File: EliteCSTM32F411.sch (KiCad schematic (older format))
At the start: 27 parts, among them SW1 Boot Mode, SW2 Reset Switch, U1 STM32F411CEUx, U2 XC6206PxxxMR, U3 Elite-C, Y1 8Mhz 3225

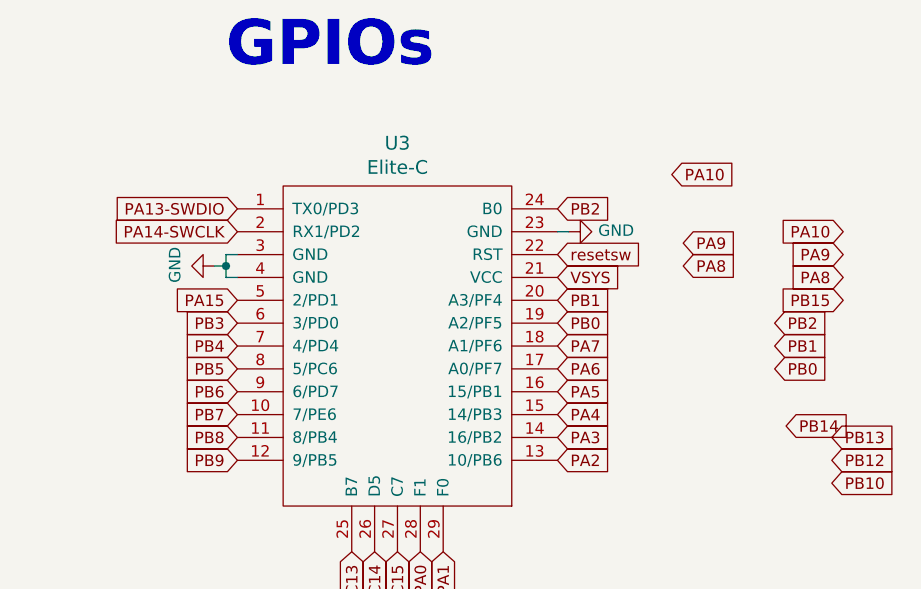
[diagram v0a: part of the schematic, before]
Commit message: redid some pins, i2c compatible with pro micro. (also redid some labels)
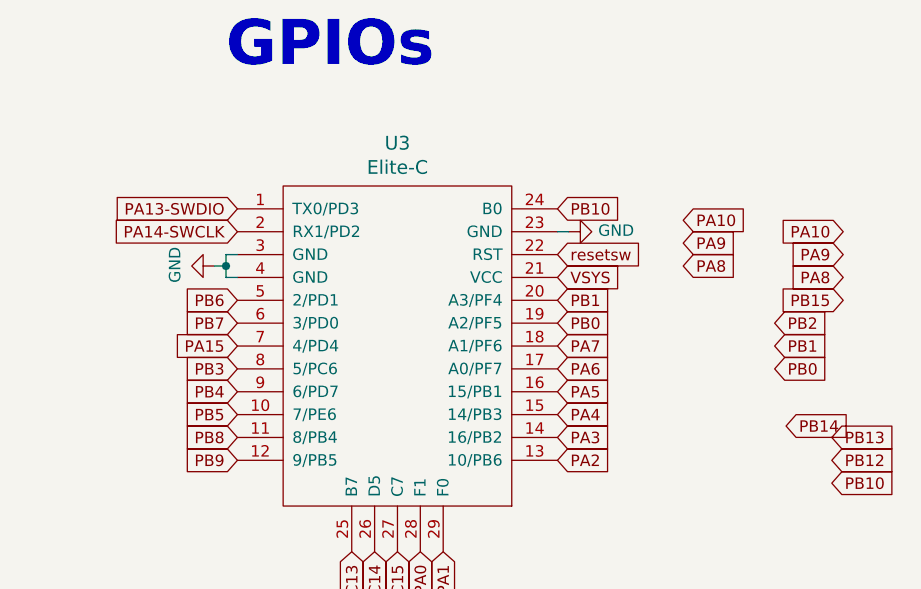
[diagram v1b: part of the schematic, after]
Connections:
- net PA15: now also U3.7 (4/PD4); no longer U3.5 (2/PD1)
- net PB10: now also U3.24 (B0)
- net PB2: no longer U3.24 (B0)
- net PB3: now also U3.8 (5/PC6); no longer U3.6 (3/PD0)
- net PB4: now also U3.9 (6/PD7); no longer U3.7 (4/PD4)
- net PB5: now also U3.10 (7/PE6); no longer U3.8 (5/PC6)
- net PB6: now also U3.5 (2/PD1); no longer U3.9 (6/PD7)
- net PB7: now also U3.6 (3/PD0); no longer U3.10 (7/PE6)
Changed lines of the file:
@@
 Text GLabel 5600 7400 0    50   Input ~ 0
 PA14-SWCLK
+Text GLabel 5600 7900 0    50   Input ~ 0
+PA15
+Text GLabel 5600 8000 0    50   Input ~ 0
+PB3
+Text GLabel 5600 8100 0    50   Input ~ 0
+PB4
+Text GLabel 5600 8200 0    50   Input ~ 0
+PB5
 Text GLabel 5600 7700 0    50   Input ~ 0
-PA15
+PB6
 Text GLabel 5600 7800 0    50   Input ~ 0
-PB3
-Text GLabel 5600 7900 0    50   Input ~ 0
-PB4
-Text GLabel 5600 8000 0    50   Input ~ 0
-PB5
-Text GLabel 5600 8100 0    50   Input ~ 0
-PB6
-Text GLabel 5600 8200 0    50   Input ~ 0
 PB7
 Text GLabel 2200 9350 0    50   Input ~ 0
@@
 Text GLabel 7550 7450 2    50   Input ~ 0
 PA9
-Text GLabel 7500 7150 2    50   Input ~ 0
+Text GLabel 7550 7350 2    50   Input ~ 0
 PA10
 Text GLabel 7000 7800 2    50   Input ~ 0
@@
 Text GLabel 7000 7700 2    50   Input ~ 0
 PB1
-Text GLabel 7000 7300 2    50   Input ~ 0
-PB2
 $Comp
 L Connector:TestPoint TP1
@@
 Text GLabel 850  4250 2    50   Input ~ 0
 boot0
+Text GLabel 7000 7300 2    50   Input ~ 0
+PB10
 $EndSCHEMATC
